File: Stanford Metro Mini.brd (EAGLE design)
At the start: 17.8 x 43.2 mm, 28 parts, among them J1 MICRO-USB-B-TYPE, SW1 KMR231NGLFS, U1 FT231XQ, U2 MIC5225-5.0, U3 ATmega328P-MU, Y1 CSTCE16M0V53-R0

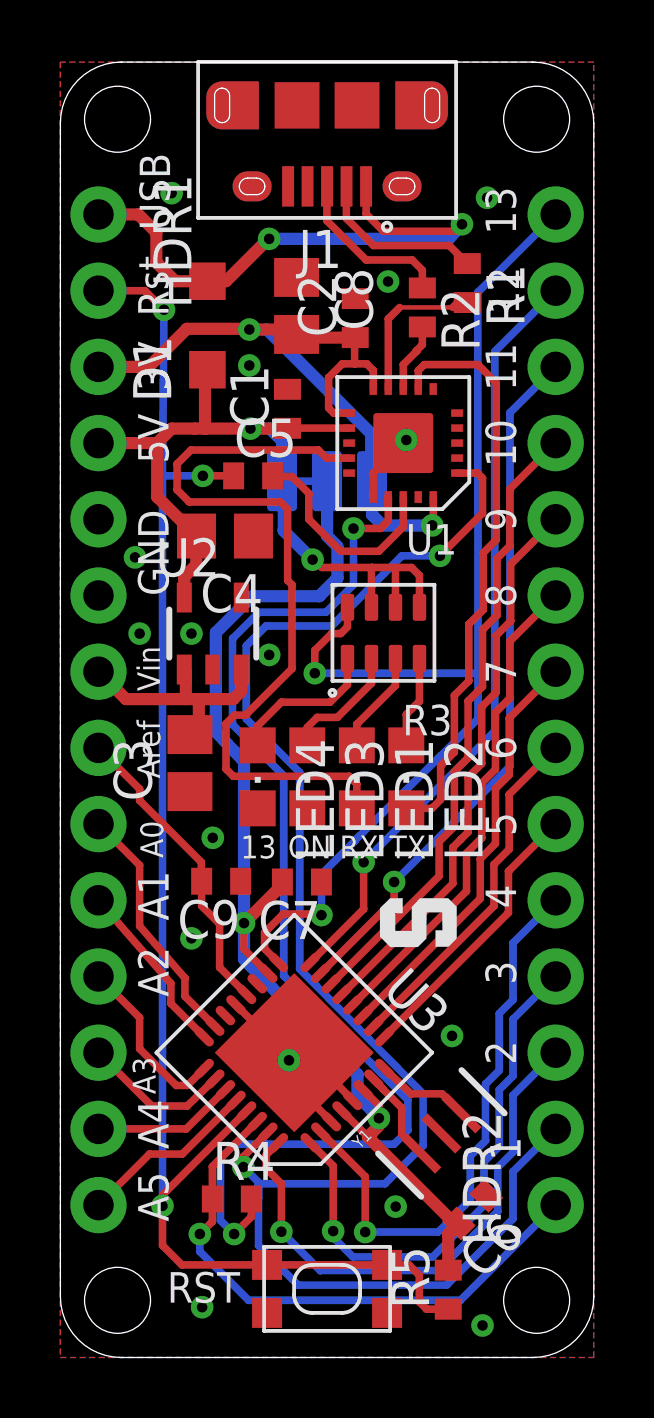
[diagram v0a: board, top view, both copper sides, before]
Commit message: Fixed issues with first board run
Fixed solder paste
Adjusted QFN pad sizes
Added the cam file to make regenerating gerbers easier
Regenerated gerbers
Generated SVGs of solder paste layer for laser cutting stencils
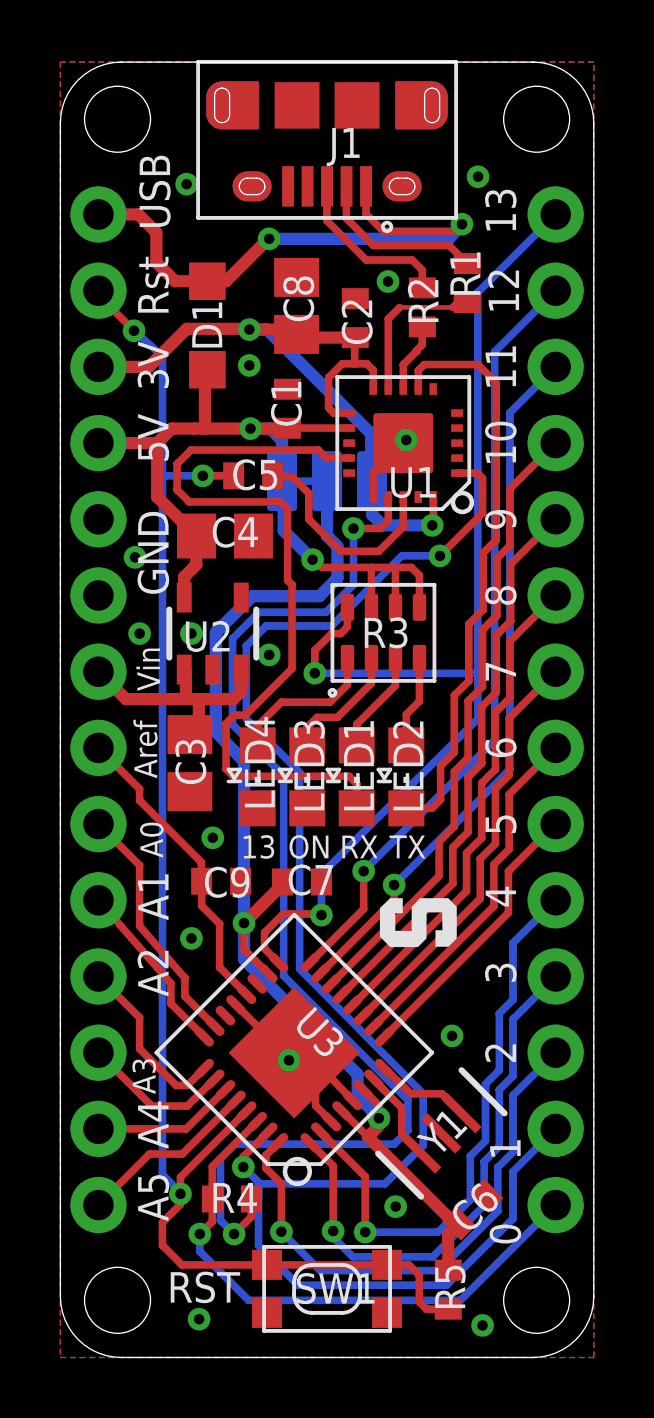
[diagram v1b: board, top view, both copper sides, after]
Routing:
- net RESET: track 51.3 -> 50.2 mm
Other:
- board text added: "SW1"
